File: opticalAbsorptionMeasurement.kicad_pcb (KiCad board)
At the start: 2 copper layers, 169 parts, among them J1 Conn_01x02_Male, J2 Conn_01x02_Male, J3 Conn_01x03_Male, J4 Conn_01x03_Male, J5 Conn_01x03_Male, J6 Conn_01x03_Male, J7 Conn_01x02_Male, J8 Conn_01x02_Male, J9 Conn_01x02_Male, Q1 J111, Q2 J111, Q3 J111, Q4 J111, U1 TEN5-0523, U10 ADR01, U11 OPA602AU, U12 OPA602AU, U13 OPA602AU, U14 OPA602AU, U15 OPA602AU, U16 OPA602AU, U19 OPA602AU, U2 OPA602AU, U20 OPA602AU, U21 OPA602AU, U22 OPA602AU, U23 OPA602AU, U24 OPA602AU, U3 OPA602AU, U6 L7812, U7 L7912, U8 OPA602AU, U9 OPA602AU

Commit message: update resistor
update resistor
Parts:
- added R39: 10k, Resistor_THT:R_Axial_DIN0207_L6.3mm_D2.5mm_P10.16mm_Horizontal, F.Cu at (91.8, 71.6)
- added R40: 10k, Resistor_THT:R_Axial_DIN0207_L6.3mm_D2.5mm_P10.16mm_Horizontal, F.Cu at (91.8, 57.6)
- moved J8 8.80 mm to (132.2, 111.2), turned to 90 degrees
- moved C18 5.03 mm to (99.8, 79.2)
- moved C13 4.93 mm to (109.9, 63.9)
- moved C19 4.43 mm to (100.5, 64.6)
- moved C12 4.09 mm to (108.0, 78.8)
- moved U7 3.23 mm to (116.4, 61.8)
- moved U6 1.68 mm to (113.9, 78.5)
- moved R34 1.02 mm to (173.3, 179.5)
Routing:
- net -12V: track 742.1 -> 747.3 mm
- net -15V: track 37.0 -> 41.3 mm
- net +15V: track 29.9 -> 34.1 mm
- net V3: track 27.4 -> 29.5 mm
- net +5V: track 232.2 -> 234.3 mm
- net Net-(R12-Pad1): track 21.0 -> 22.7 mm
- net RW2: track 19.1 -> 20.7 mm
- net Net-(C76-Pad1): track 27.4 -> 26.3 mm
- net +12V: track 714.7 -> 715.8 mm
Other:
- board outline added: 160 x 160 mm
- board text added: "https://github.com/Johann-Schmid/opticalAbsorptionMeasurement"

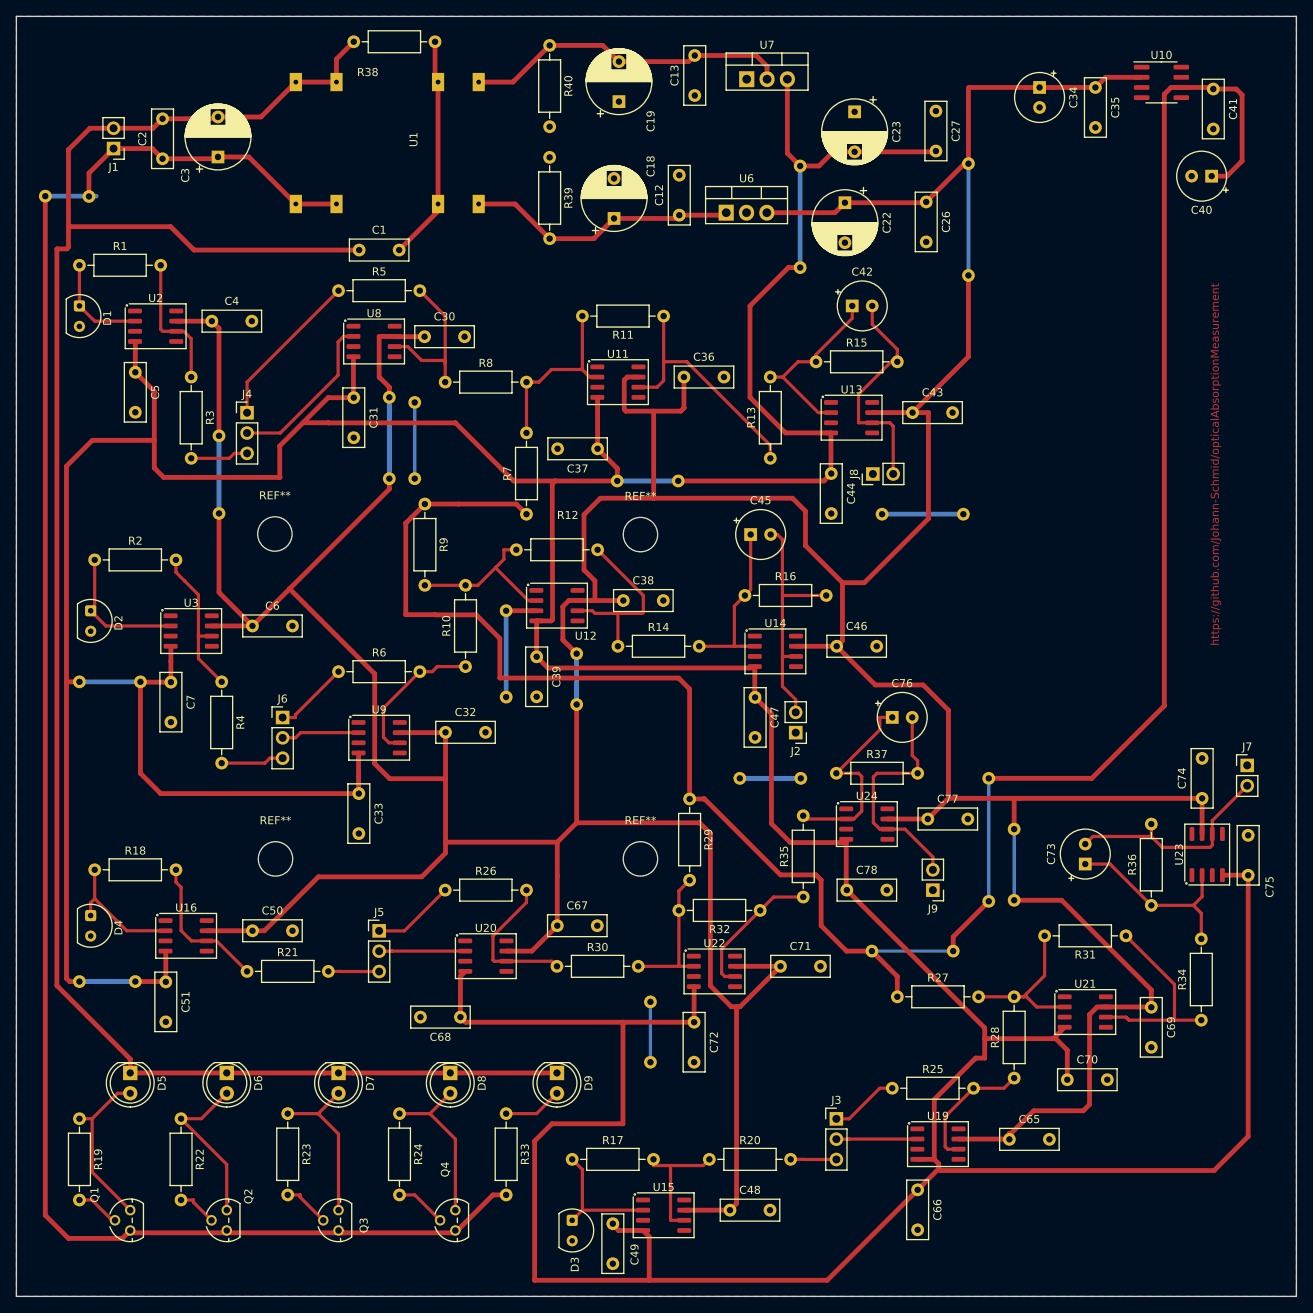
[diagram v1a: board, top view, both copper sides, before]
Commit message: change pin distance TEN5-0523
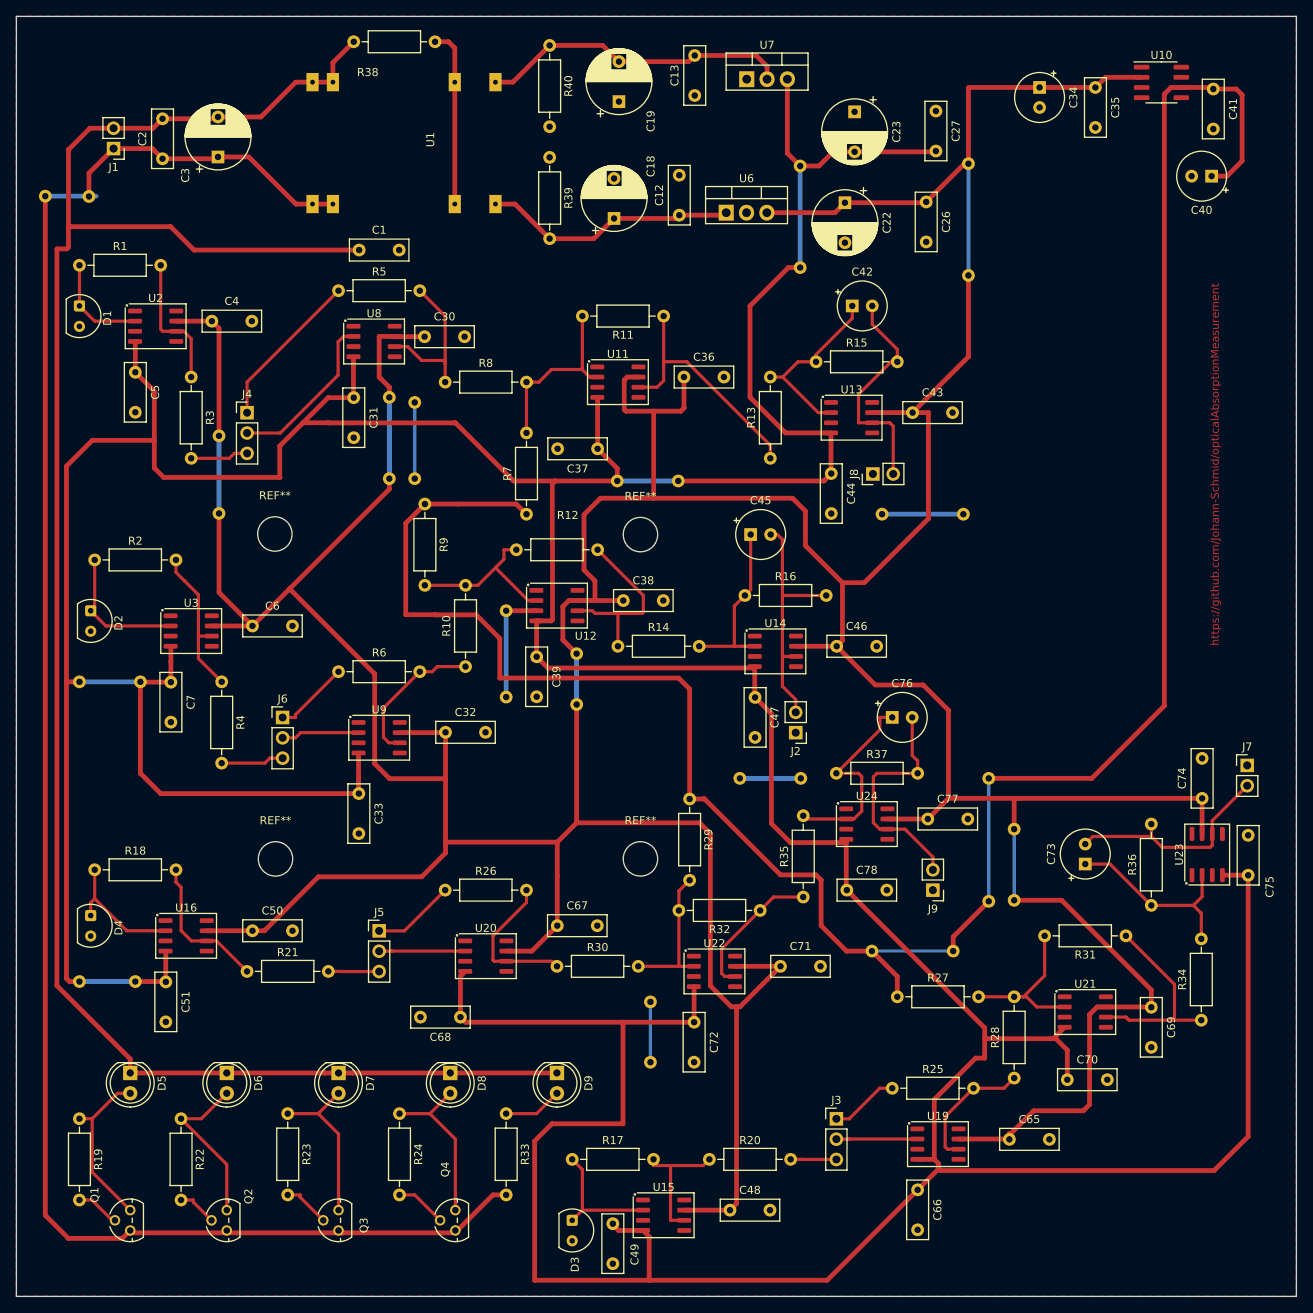
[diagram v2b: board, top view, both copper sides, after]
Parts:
- moved U1 2.09 mm to (90.1, 80.0)
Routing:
- net GND: track 77.6 -> 71.7 mm
- net +15V: track 34.1 -> 32.0 mm
- net -15V: track 41.3 -> 39.2 mm
